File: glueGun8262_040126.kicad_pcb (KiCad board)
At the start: 2 copper layers, 56 parts, among them CN1 KF243-5.0-2P, CN2 KF243-5.0-2P, CN3 KF243-5.0-2P, CN4 KF243-5.0-2P, CN5 KF243-5.0-2P, CN6 KF243-5.0-2P, CN7 KF243-5.0-2P, CN9 KF243-5.0-4P, U1 DRV8262DDWR, U10 INA240A2DR, U11 INA240A2DR, U2 DRV8262DDWR, U3 ESP32-S3-DEVKITC-1-N8R2, U5 6N137, U6 INA240A2DR, U7 INA240A2DR, U8 K7805-1000R3_C2992391, U9 TLP281-4(GB-TP,J,F

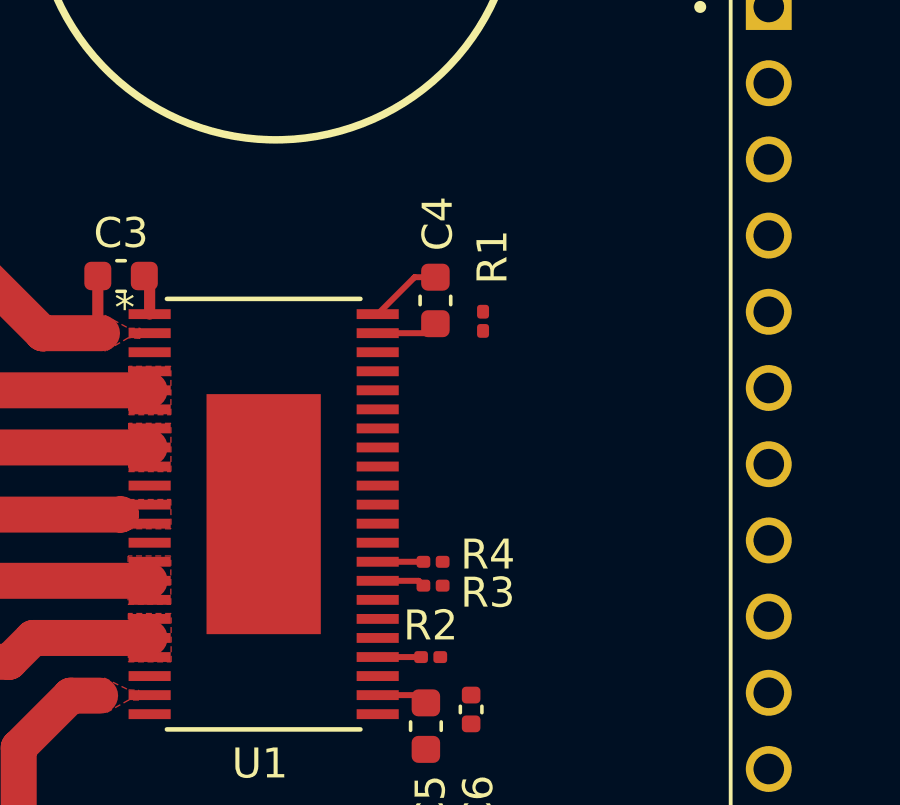
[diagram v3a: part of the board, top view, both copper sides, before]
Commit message: in the process of changing 0402 to 0603 footprints
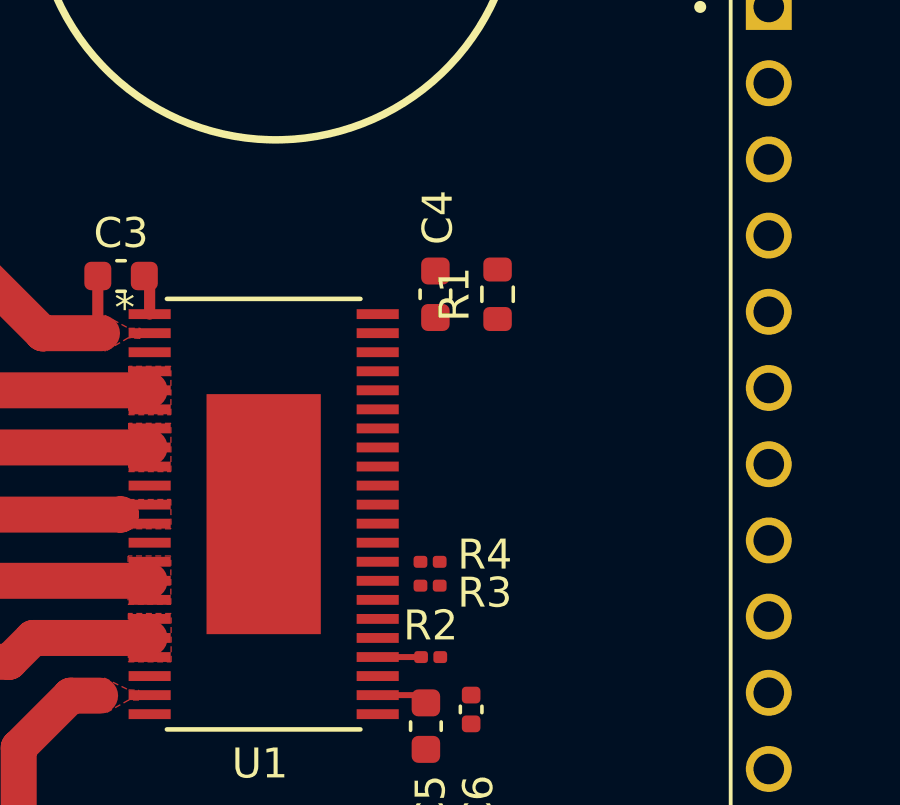
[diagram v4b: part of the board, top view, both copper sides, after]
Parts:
- R1: footprint Resistor_SMD:R_0201_0603Metric -> Resistor_SMD:R_0603_1608Metric
- moved R1 1.02 mm to (157.2, 71.2)
- moved C4 0.21 mm to (155.2, 71.2)
- moved R3 0.10 mm to (155.0, 81.0)
- moved R4 0.10 mm to (155.0, 80.2)
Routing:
- net Net-(U1-CPH/GND): track 2.43 -> 0.00 mm
- net Net-(U1-CPL/DVDD): track 2.08 -> 0.00 mm
- net Net-(U1-IPROPI/DECAY): track 1.59 -> 0.00 mm
- net Net-(U1-IPROPI/RSVD): track 1.53 -> 0.00 mm
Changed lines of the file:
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@@
 		)
 	)
-	(footprint "Resistor_SMD:R_0201_0603Metric"
+	(footprint "Resistor_SMD:R_0603_1608Metric"
 		(layer "F.Cu")
-		(at 156.765625 72.151875 90)
-		(descr "Resistor SMD 0201 (0603 Metric), square (rectangular) end terminal, IPC-7351 nominal, (Body size source: https://www.vishay.com/docs/20052/crcw0201e3.pdf), generated with kicad-footprint-generator")
+		(at 157.25 71.25 90)
+		(descr "Resistor SMD 0603 (1608 Metric), square (rectangular) end terminal, IPC-7351 nominal, (Body size source: IPC-SM-782 page 72, https://www.pcb-3d.com/wordpress/wp-content/uploads/ipc-sm-782a_amendment_1_and_2.pdf), generated with kicad-footprint-generator")
 		(tags "resistor")
 		(property "Reference" "R1"
-			(at 2.143125 0.3175 90)
+			(at 0 -1.43 90)
 			(layer "F.SilkS")
 			(effects
@@
 		)
 		(property "Value" "10k"
-			(at 0 1.05 90)
+			(at 0 1.43 90)
 			(layer "F.Fab")
 			(effects
@@
 			)
 		)
-		(property "Description" "Resistor"
+		(property "Description" ""
 			(at 0 0 90)
 			(layer "F.Fab")
@@
 			)
 		)
-		(property "lcsc" "C84376"
+		(property "lcsc" ""
 			(at 0 0 90)
 			(unlocked yes)
@@
 		(attr smd)
 		(fp_line
-			(start 0.7 -0.35)
-			(end 0.7 0.35)
+			(start -0.237258 -0.5225)
+			(end 0.237258 -0.5225)
+			(stroke
+				(width 0.12)
+				(type solid)
+			)
+			(layer "F.SilkS")
+		)
+		(fp_line
+			(start -0.237258 0.5225)
+			(end 0.237258 0.5225)
+			(stroke
+				(width 0.12)
+				(type solid)
+			)
+			(layer "F.SilkS")
+		)
+		(fp_line
+			(start 1.48 -0.73)
+			(end 1.48 0.73)
 			(stroke
 				(width 0.05)
@@
 		)
 		(fp_line
-			(start -0.7 -0.35)
-			(end 0.7 -0.35)
+			(start -1.48 -0.73)
+			(end 1.48 -0.73)
 			(stroke
 				(width 0.05)
@@
 		)
 		(fp_line
-			(start 0.7 0.35)
-			(end -0.7 0.35)
+			(start 1.48 0.73)
+			(end -1.48 0.73)
 			(stroke
 				(width 0.05)
@@
 		)
 		(fp_line
-			(start -0.7 0.35)
-			(end -0.7 -0.35)
+			(start -1.48 0.73)
+			(end -1.48 -0.73)
 			(stroke
 				(width 0.05)
@@
 		)
 		(fp_line
-			(start 0.3 -0.15)
-			(end 0.3 0.15)
+			(start 0.8 -0.4125)
+			(end 0.8 0.4125)
 			(stroke
 				(width 0.1)
@@
 		)
 		(fp_line
-			(start -0.3 -0.15)
-			(end 0.3 -0.15)
+			(start -0.8 -0.4125)
+			(end 0.8 -0.4125)
 			(stroke
 				(width 0.1)
@@
 		)
 		(fp_line
-			(start 0.3 0.15)
-			(end -0.3 0.15)
+			(start 0.8 0.4125)
+			(end -0.8 0.4125)
 			(stroke
 				(width 0.1)
@@
 		)
 		(fp_line
-			(start -0.3 0.15)
-			(end -0.3 -0.15)
+			(start -0.8 0.4125)
+			(end -0.8 -0.4125)
 			(stroke
 				(width 0.1)
@@
 		)
 		(fp_text user "${REFERENCE}"
-			(at 0 -0.68 90)
+			(at 0 0 90)
 			(layer "F.Fab")
 			(effects
 				(font
-					(size 0.25 0.25)
-					(thickness 0.04)
+					(size 0.4 0.4)
+					(thickness 0.06)
 				)
 			)
 		)
-		(pad "" smd roundrect
-			(at -0.345 0 90)
-			(size 0.318 0.36)
-			(layers "F.Paste")
-			(roundrect_rratio 0.25)
-		)
-		(pad "" smd roundrect
-			(at 0.345 0 90)
-			(size 0.318 0.36)
-			(layers "F.Paste")
-			(roundrect_rratio 0.25)
-		)
 		(pad "1" smd roundrect
-			(at -0.32 0 90)
-			(size 0.46 0.4)
-			(layers "F.Cu" "F.Mask")
+			(at -0.825 0 90)
+			(size 0.8 0.95)
+			(layers "F.Cu" "F.Mask" "F.Paste")
 			(roundrect_rratio 0.25)
 			(net 14 "/nSLEEP")
@@
 		)
 		(pad "2" smd roundrect
-			(at 0.32 0 90)
-			(size 0.46 0.4)
-			(layers "F.Cu" "F.Mask")
+			(at 0.825 0 90)
+			(size 0.8 0.95)
+			(layers "F.Cu" "F.Mask" "F.Paste")
 			(roundrect_rratio 0.25)
 			(net 1 "GND")
@@
 		)
 		(embedded_fonts no)
-		(model "${KICAD9_3DMODEL_DIR}/Resistor_SMD.3dshapes/R_0201_0603Metric.step"
+		(model "${KICAD9_3DMODEL_DIR}/Resistor_SMD.3dshapes/R_0603_1608Metric.step"
 			(offset
 				(xyz 0 0 0)
@@
 	(footprint "Resistor_SMD:R_0201_0603Metric"
 		(layer "F.Cu")
-		(at 155.09875 80.9625)
+		(at 155 80.9625)
 		(descr "Resistor SMD 0201 (0603 Metric), square (rectangular) end terminal, IPC-7351 nominal, (Body size source: https://www.vishay.com/docs/20052/crcw0201e3.pdf), generated with kicad-footprint-generator")
 		(tags "resistor")
@@
 	(footprint "Capacitor_SMD:C_0603_1608Metric"
 		(layer "F.Cu")
-		(at 155.178125 71.45625 -90)
+		(at 155.178125 71.25 -90)
 		(descr "Capacitor SMD 0603 (1608 Metric), square (rectangular) end terminal, IPC-7351 nominal, (Body size source: IPC-SM-782 page 76, https://www.pcb-3d.com/wordpress/wp-content/uploads/ipc-sm-782a_amendment_1_and_2.pdf), generated with kicad-footprint-generator")
 		(tags "capacitor")
@@
 	(footprint "Resistor_SMD:R_0201_0603Metric"
 		(layer "F.Cu")
-		(at 155.09875 80.16875)
+		(at 155 80.16875)
 		(descr "Resistor SMD 0201 (0603 Metric), square (rectangular) end terminal, IPC-7351 nominal, (Body size source: https://www.vishay.com/docs/20052/crcw0201e3.pdf), generated with kicad-footprint-generator")
 		(tags "resistor")
@@
 	)
 	(segment
-		(start 154.485073 70.68125)
-		(end 155.178125 70.68125)
-		(width 0.2)
-		(layer "F.Cu")
-		(net 4)
-	)
-	(segment
-		(start 153.254399 71.911924)
-		(end 154.485073 70.68125)
-		(width 0.2)
-		(layer "F.Cu")
-		(net 4)
-	)
-	(segment
-		(start 155.478701 72.546924)
-		(end 155.495625 72.53)
-		(width 0.2)
-		(layer "F.Cu")
-		(net 5)
-	)
-	(segment
-		(start 153.254399 72.546924)
-		(end 154.862451 72.546924)
-		(width 0.2)
-		(layer "F.Cu")
-		(net 5)
-	)
-	(segment
-		(start 154.862451 72.546924)
-		(end 155.178125 72.23125)
-		(width 0.2)
-		(layer "F.Cu")
-		(net 5)
-	)
-	(segment
 		(start 154.601924 84.611924)
 		(end 154.860625 84.870625)
@@
 	)
 	(segment
-		(start 154.618174 80.801924)
-		(end 154.77875 80.9625)
-		(width 0.2)
-		(layer "F.Cu")
-		(net 16)
-	)
-	(segment
-		(start 153.254399 80.801924)
-		(end 154.618174 80.801924)
-		(width 0.2)
-		(layer "F.Cu")
-		(net 16)
-	)
-	(segment
-		(start 154.776924 80.166924)
-		(end 154.77875 80.16875)
-		(width 0.2)
-		(layer "F.Cu")
-		(net 17)
-	)
-	(segment
-		(start 153.254399 80.166924)
-		(end 154.776924 80.166924)
-		(width 0.2)
-		(layer "F.Cu")
-		(net 17)
-	)
-	(segment

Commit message: cont rearrange pcb
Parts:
- C10, C6: footprint Capacitor_SMD:C_0402_1005Metric -> Capacitor_SMD:C_0603_1608Metric
- R11, R2, R3, R4, R5, R6: footprint Resistor_SMD:R_0201_0603Metric -> Resistor_SMD:R_0603_1608Metric
- R14: footprint Resistor_SMD:R_0402_1005Metric -> Resistor_SMD:R_0603_1608Metric
- moved R14 13.8 mm to (193.4, 104.0)
- moved U3 10.2 mm to (178.1, 81.4)
- moved CN9 5.43 mm to (218.7, 108.9)
- moved CN6 5.29 mm to (218.7, 71.9)
- moved D1 5.15 mm to (208.0, 92.2)
- moved U5 5.15 mm to (200.7, 93.2)
- moved R11 5.15 mm to (204.0, 91.0)
- moved U8 5.15 mm to (204.6, 70.7)
- moved CN7 5.15 mm to (218.7, 90.6)
- moved C16 4.86 mm to (196.4, 72.8)
- moved C17 4.86 mm to (196.3, 67.5)
- moved D2 4.55 mm to (203.3, 116.3)
- moved D4 4.55 mm to (203.3, 106.1)
- moved R16 4.55 mm to (208.5, 101.3)
- moved D3 4.55 mm to (203.3, 111.2)
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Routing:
- net +48V: track 275.5 -> 0.00 mm
- net /U2_OUT2: track 29.9 -> 0.00 mm
- net /U1_OUT4: track 28.9 -> 0.00 mm
- net /U2_OUT4: track 28.0 -> 0.00 mm
- net /U1_OUT2: track 28.0 -> 0.00 mm
- net Net-(U10-IN-): track 26.4 -> 0.00 mm
- net Net-(U7-IN-): track 21.6 -> 0.00 mm
- net Net-(U6-IN-): track 21.4 -> 0.00 mm
- net /U1_OUT1: track 21.0 -> 0.00 mm
- net Net-(U11-IN-): track 20.2 -> 0.00 mm
- net /U2_OUT1: track 18.3 -> 0.00 mm
- net /U2_OUT3: track 15.4 -> 0.00 mm
- net /U1_OUT3: track 14.8 -> 0.00 mm
- net +3V3: track 6.51 -> 0.00 mm
- net Net-(U2-CPH/GND): track 2.27 -> 0.00 mm
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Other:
- board outline added: 126.8 x 85.6 mm

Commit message: cont
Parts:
- moved C1 61.2 mm to (155.2, 119.1)
- moved CN1 61.2 mm to (120.6, 118.5)
- moved C21 15.6 mm to (138.4, 103.7)
- moved U11 14.5 mm to (132.8, 105.2)
- moved R20 14.5 mm to (132.8, 99.8)
- moved C2 14.3 mm to (137.4, 118.7)
- moved U10 14.1 mm to (132.8, 84.4)
- moved R19 14.1 mm to (132.8, 89.9)
- moved C20 13.9 mm to (138.1, 84.1)
- moved C10 13.8 mm to (156.4, 100.4)
- moved C7 13.8 mm to (144.7, 86.0)
- moved C9 13.8 mm to (155.0, 100.9)
- moved R5 13.8 mm to (156.1, 95.6)
- moved R6 13.8 mm to (155.8, 93.0)
- moved C8 13.8 mm to (153.7, 85.9)
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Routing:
- net +48V: track 0.00 -> 250.8 mm
- net /U2_OUT2: track 0.00 -> 25.3 mm
- net /U1_OUT2: track 0.00 -> 23.8 mm
- net /U2_OUT4: track 0.00 -> 23.6 mm
- net /U1_OUT4: track 0.00 -> 23.2 mm
- net /U2_OUT3: track 0.00 -> 10.3 mm
- net Net-(U10-IN-): track 0.00 -> 10.2 mm
- net /U1_OUT3: track 0.00 -> 9.67 mm
- net /U2_OUT1: track 0.00 -> 9.66 mm
- net /U1_OUT1: track 0.00 -> 9.59 mm
- net Net-(U6-IN-): track 0.00 -> 9.58 mm
- net Net-(U7-IN-): track 0.00 -> 8.92 mm
- net Net-(U11-IN-): track 0.00 -> 8.65 mm
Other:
- board size 126.8 x 85.6 mm -> 126.8 x 84.5 mm

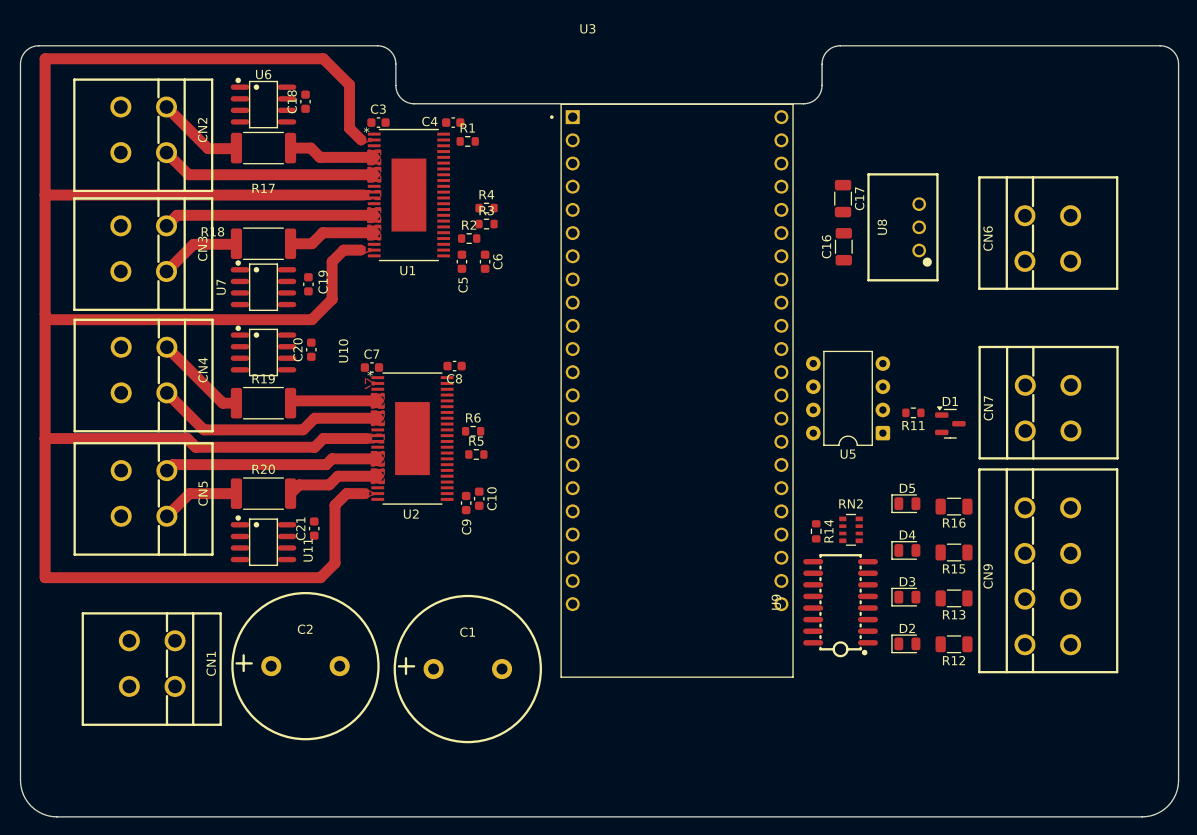
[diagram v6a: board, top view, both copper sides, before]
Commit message: high power routed and locked
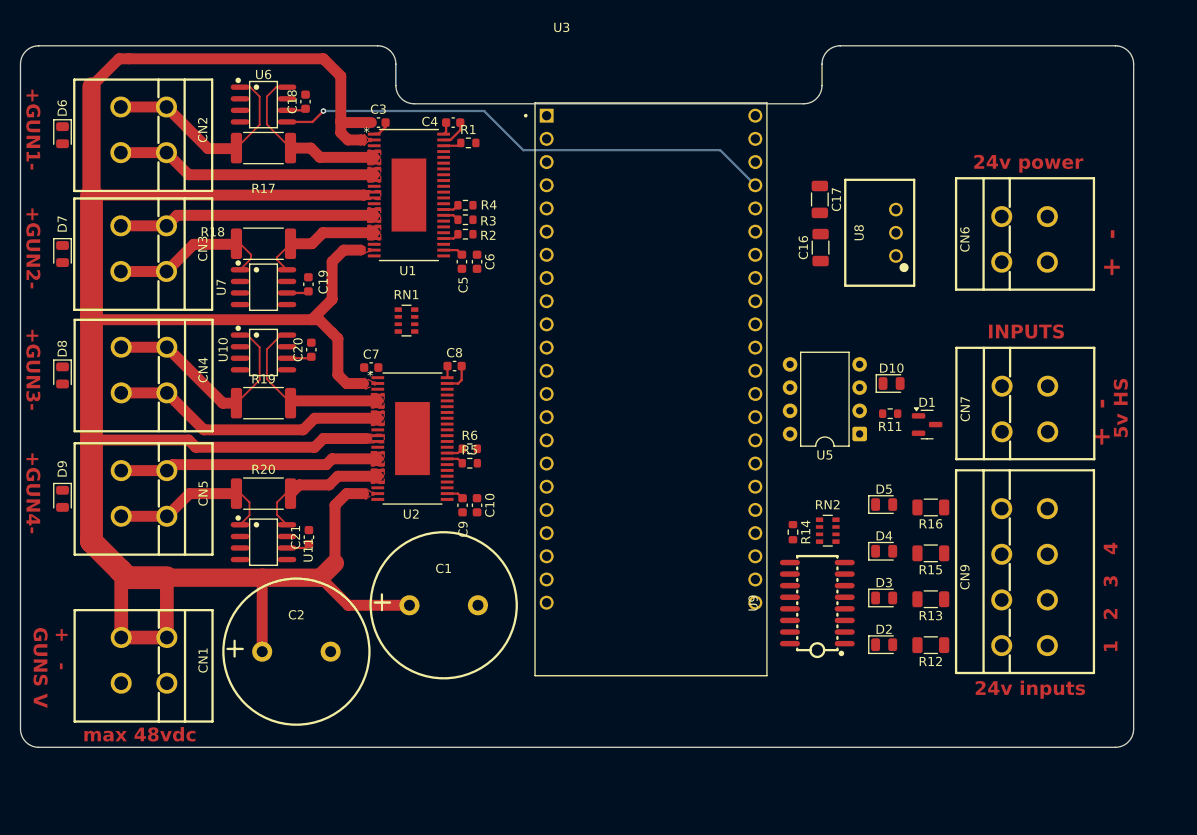
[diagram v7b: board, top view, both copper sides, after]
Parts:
- added D10: green, LED_SMD:LED_0805_2012Metric, F.Cu at (201.6, 87.8)
- added D6: red, LED_SMD:LED_0805_2012Metric, F.Cu at (110.8, 60.6)
- added D7: red, LED_SMD:LED_0805_2012Metric, F.Cu at (110.8, 73.6)
- added D8: red, LED_SMD:LED_0805_2012Metric, F.Cu at (110.8, 86.9)
- added D9: red, LED_SMD:LED_0805_2012Metric, F.Cu at (110.8, 100.4)
- added RN1: 470r, Resistor_SMD:R_Array_Convex_4x0603, F.Cu at (148.5, 80.9)
- R11: value 470r -> 150r
- moved C1 7.47 mm to (152.6, 112.1)
- moved U3 2.86 mm to (175.3, 88.4)
- moved U8 2.61 mm to (202.1, 71.3)
- moved CN6 2.55 mm to (216.2, 72.0)
- moved CN9 2.55 mm to (216.2, 109.0)
- moved C16 2.55 mm to (193.8, 72.9)
- moved C17 2.55 mm to (193.8, 67.6)
- moved CN7 2.55 mm to (216.2, 90.6)
- moved D1 2.55 mm to (205.5, 92.3)
- moved D2 2.55 mm to (200.8, 116.4)
- moved D3 2.55 mm to (200.8, 111.3)
- moved D4 2.55 mm to (200.8, 106.2)
- moved D5 2.55 mm to (200.8, 101.0)
- moved R11 2.55 mm to (201.5, 91.1)
- moved R13 2.55 mm to (205.9, 111.4)
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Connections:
- CN7 pad 1: Net-(D1-A) -> Net-(D10-A)
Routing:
- net /Gun1Vref: track 0.00 -> 55.2 mm, vias 0 -> 1
- net +48V: track 250.8 -> 275.2 mm
- net Net-(U10-IN-): track 10.2 -> 25.0 mm
- net Net-(U6-IN-): track 9.58 -> 23.8 mm
- net +3V3: track 0.00 -> 9.84 mm
- net /U2_OUT1: track 9.66 -> 19.5 mm
- net Net-(U11-IN-): track 8.65 -> 18.4 mm
- net /U1_OUT1: track 9.59 -> 18.9 mm
- net Net-(U7-IN-): track 8.92 -> 18.2 mm
- net /U2_OUT4: track 23.6 -> 28.6 mm
- net /U2_OUT2: track 25.3 -> 30.3 mm
- net /U1_OUT4: track 23.2 -> 28.2 mm
- net /U1_OUT2: track 23.8 -> 28.8 mm
- net /U2_OUT3: track 10.3 -> 15.1 mm
- net /U1_OUT3: track 9.67 -> 13.6 mm
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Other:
- board size 126.8 x 84.5 mm -> 121.9 x 76.8 mm
- board text added: "+ -"
- board text added: "+ - GUNS V"
- board text added: "+GUN1-"
- board text added: "+GUN2-"
- board text added: "+GUN3-"
- board text added: "+GUN4-"
- board text added: "1 2 3 4"
- board text added: "24v inputs"
- board text added: "24v power"
- board text added: "5v HS"
- board text added: "INPUTS"
- board text added: "max 48vdc"

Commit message: no drc errors1
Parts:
- moved D10 6.59 mm to (204.7, 93.6)
- moved D1 2.29 mm to (205.2, 90.0)
- moved C7 0.63 mm to (144.6, 85.4)
- moved R4 0.51 mm to (155.1, 67.8)
- moved R2 0.51 mm to (155.1, 71.0)
- moved R3 0.51 mm to (155.1, 69.4)
- moved R11 0.45 mm to (201.2, 90.7)
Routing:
- net +3V3: track 9.84 -> 237.1 mm, vias 0 -> 7
- net +5V: track 0.00 -> 79.5 mm, vias 0 -> 2
- net /Gun2Vref: track 0.00 -> 66.5 mm, vias 0 -> 6
- net /nSLEEP: track 2.01 -> 52.0 mm, vias 0 -> 2
- net /Input_1_24v: track 0.00 -> 48.9 mm, vias 0 -> 2
- net Net-(D6-A): track 0.00 -> 48.8 mm, vias 0 -> 2
- net Net-(D9-A): track 0.00 -> 47.6 mm, vias 0 -> 2
- net /nFAULT: track 1.76 -> 48.6 mm, vias 0 -> 4
- net /Input_2_24v: track 0.00 -> 44.3 mm, vias 0 -> 2
- net Net-(D8-A): track 0.00 -> 44.2 mm, vias 0 -> 4
- net Net-(D7-A): track 0.00 -> 42.0 mm, vias 0 -> 4
- net /U1_IN1: track 0.00 -> 39.0 mm, vias 0 -> 1
- net /Gun4Vref: track 0.00 -> 37.2 mm, vias 0 -> 3
- net /U1_IN3: track 0.00 -> 35.1 mm, vias 0 -> 1
- net /Gun3Vref: track 0.00 -> 32.4 mm, vias 0 -> 2
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- added copper zone on B.Cu, net GND
- added copper zone on F.Cu, net GND
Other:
- outline, holes or cut-outs redrawn
